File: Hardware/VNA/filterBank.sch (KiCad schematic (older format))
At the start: 18 parts, among them U10 SN74LVC1G139, U11 PE42440, U8 74AHC1G04, U9 PE42440

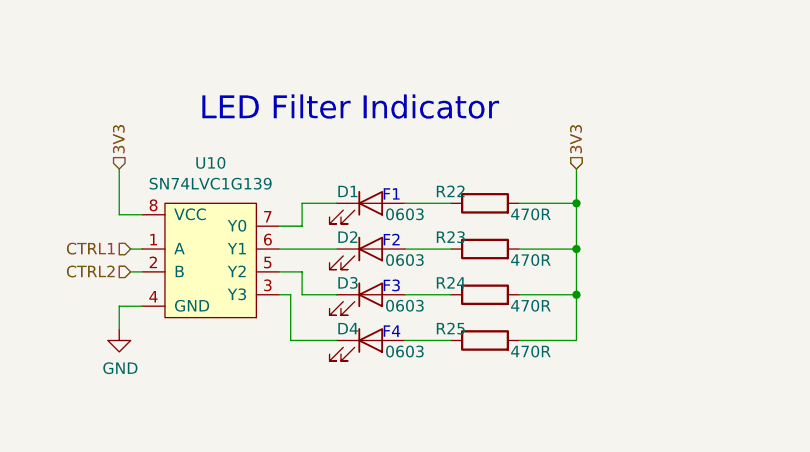
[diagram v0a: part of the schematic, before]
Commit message: added footprints and 3d models
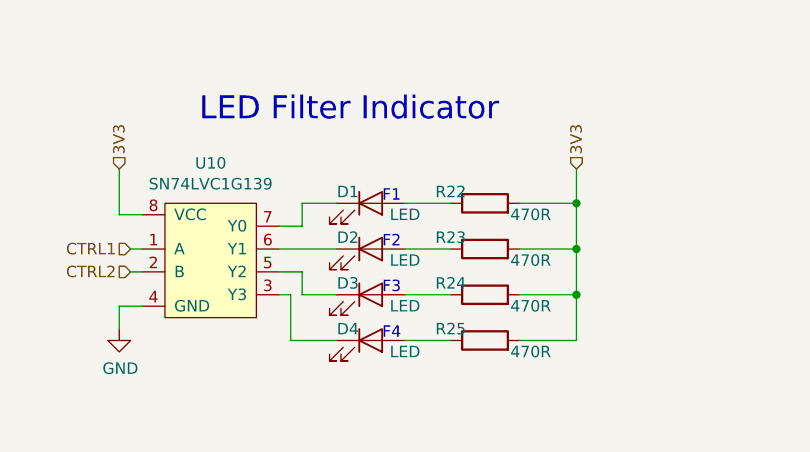
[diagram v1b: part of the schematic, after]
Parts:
- D1, D2, D3, D4: value 0603 -> LED; footprint (none) -> LED_SMD:LED_0603_1608Metric
- R22, R23, R24, R25: footprint (none) -> Resistor_SMD:R_0603_1608Metric
- U10: footprint (none) -> VNA_Footprints:VSSOP-8_2.9x3.15mm_P0.65
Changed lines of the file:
@@
 	8100 3150 8200 3150
 $Comp
-L power:GND #PWR061
+L power:GND #PWR060
 U 1 1 5C2A3D55
 P 8700 3200
-F 0 "#PWR061" H 8700 2950 50  0001 C CNN
+F 0 "#PWR060" H 8700 2950 50  0001 C CNN
 F 1 "GND" H 8705 3027 50  0000 C CNN
 F 2 "" H 8700 3200 50  0001 C CNN
@@
 	8750 1850 8750 1950
 $Comp
-L power:GND #PWR062
+L power:GND #PWR061
 U 1 1 5C2A413F
 P 8750 1950
-F 0 "#PWR062" H 8750 1700 50  0001 C CNN
+F 0 "#PWR061" H 8750 1700 50  0001 C CNN
 F 1 "GND" H 8755 1777 50  0000 C CNN
 F 2 "" H 8750 1950 50  0001 C CNN
@@
 	3600 3100 3500 3100
 $Comp
-L power:GND #PWR054
+L power:GND #PWR053
 U 1 1 5C2A4744
 P 3000 3150
-F 0 "#PWR054" H 3000 2900 50  0001 C CNN
+F 0 "#PWR053" H 3000 2900 50  0001 C CNN
 F 1 "GND" H 3005 2977 50  0000 C CNN
 F 2 "" H 3000 3150 50  0001 C CNN
@@
 	3550 1800 3550 1900
 $Comp
-L power:GND #PWR055
+L power:GND #PWR054
 U 1 1 5C2A475D
 P 3550 1900
-F 0 "#PWR055" H 3550 1650 50  0001 C CNN
+F 0 "#PWR054" H 3550 1650 50  0001 C CNN
 F 1 "GND" H 3555 1727 50  0000 C CNN
 F 2 "" H 3550 1900 50  0001 C CNN
@@
 	1500 7100 1500 7200
 $Comp
-L power:GND #PWR053
+L power:GND #PWR052
 U 1 1 5C2BF9CA
 P 1500 7200
-F 0 "#PWR053" H 1500 6950 50  0001 C CNN
+F 0 "#PWR052" H 1500 6950 50  0001 C CNN
 F 1 "GND" H 1505 7027 50  0000 C CNN
 F 2 "" H 1500 7200 50  0001 C CNN
@@
 	5250 2550 5250 2600
 $Comp
-L power:GND #PWR057
+L power:GND #PWR056
 U 1 1 5C3B9385
 P 5250 2600
-F 0 "#PWR057" H 5250 2350 50  0001 C CNN
+F 0 "#PWR056" H 5250 2350 50  0001 C CNN
 F 1 "GND" H 5255 2427 50  0000 C CNN
 F 2 "" H 5250 2600 50  0001 C CNN
@@
 	5250 3250 5250 3300
 $Comp
-L power:GND #PWR058
+L power:GND #PWR057
 U 1 1 5C3B9438
 P 5250 3300
-F 0 "#PWR058" H 5250 3050 50  0001 C CNN
+F 0 "#PWR057" H 5250 3050 50  0001 C CNN
 F 1 "GND" H 5255 3127 50  0000 C CNN
 F 2 "" H 5250 3300 50  0001 C CNN
@@
 	5250 3950 5250 4000
 $Comp
-L power:GND #PWR059
+L power:GND #PWR058
 U 1 1 5C3BCF2E
 P 5250 4000
-F 0 "#PWR059" H 5250 3750 50  0001 C CNN
+F 0 "#PWR058" H 5250 3750 50  0001 C CNN
 F 1 "GND" H 5255 3827 50  0000 C CNN
 F 2 "" H 5250 4000 50  0001 C CNN
@@
 	5250 4700 5250 4750
 $Comp
-L power:GND #PWR060
+L power:GND #PWR059
 U 1 1 5C3C0D3B
 P 5250 4750
-F 0 "#PWR060" H 5250 4500 50  0001 C CNN
+F 0 "#PWR059" H 5250 4500 50  0001 C CNN
 F 1 "GND" H 5255 4577 50  0000 C CNN
 F 2 "" H 5250 4750 50  0001 C CNN
@@
 F 0 "U10" H 4600 7325 50  0000 C CNN
 F 1 "SN74LVC1G139" H 4600 7234 50  0000 C CNN
-F 2 "" H 4700 7150 100 0001 C CNN
+F 2 "VNA_Footprints:VSSOP-8_2.9x3.15mm_P0.65" H 4700 7150 100 0001 C CNN
 F 3 "" H 4700 7150 100 0001 C CNN
 	1    4600 6900
@@
 	4200 7100 4200 7200
 $Comp
-L power:GND #PWR056
+L power:GND #PWR055
 U 1 1 5CE265C0
 P 4200 7200
-F 0 "#PWR056" H 4200 6950 50  0001 C CNN
+F 0 "#PWR055" H 4200 6950 50  0001 C CNN
 F 1 "GND" H 4205 7027 50  0000 C CNN
 F 2 "" H 4200 7200 50  0001 C CNN
@@
 F 0 "R22" V 5850 6800 50  0000 C CNN
 F 1 "470R" V 5750 6450 50  0000 C CNN
-F 2 "" V 5730 6650 50  0001 C CNN
+F 2 "Resistor_SMD:R_0603_1608Metric" V 5730 6650 50  0001 C CNN
 F 3 "~" H 5800 6650 50  0001 C CNN
 	1    5800 6650
@@
 P 5300 6650
 F 0 "D1" H 5200 6700 50  0000 C CNN
-F 1 "0603" H 5450 6600 50  0000 C CNN
-F 2 "" H 5300 6650 50  0001 C CNN
+F 1 "LED" H 5450 6600 50  0000 C CNN
+F 2 "LED_SMD:LED_0603_1608Metric" H 5300 6650 50  0001 C CNN
 F 3 "~" H 5300 6650 50  0001 C CNN
 	1    5300 6650
@@
 P 5300 6850
 F 0 "D2" H 5200 6900 50  0000 C CNN
-F 1 "0603" H 5450 6800 50  0000 C CNN
-F 2 "" H 5300 6850 50  0001 C CNN
+F 1 "LED" H 5450 6800 50  0000 C CNN
+F 2 "LED_SMD:LED_0603_1608Metric" H 5300 6850 50  0001 C CNN
 F 3 "~" H 5300 6850 50  0001 C CNN
 	1    5300 6850
@@
 P 5300 7050
 F 0 "D3" H 5200 7100 50  0000 C CNN
-F 1 "0603" H 5450 7000 50  0000 C CNN
-F 2 "" H 5300 7050 50  0001 C CNN
+F 1 "LED" H 5450 7000 50  0000 C CNN
+F 2 "LED_SMD:LED_0603_1608Metric" H 5300 7050 50  0001 C CNN
 F 3 "~" H 5300 7050 50  0001 C CNN
 	1    5300 7050
@@
 P 5300 7250
 F 0 "D4" H 5200 7300 50  0000 C CNN
-F 1 "0603" H 5450 7200 50  0000 C CNN
-F 2 "" H 5300 7250 50  0001 C CNN
+F 1 "LED" H 5450 7200 50  0000 C CNN
+F 2 "LED_SMD:LED_0603_1608Metric" H 5300 7250 50  0001 C CNN
 F 3 "~" H 5300 7250 50  0001 C CNN
 	1    5300 7250
@@
 F 0 "R23" V 5850 7000 50  0000 C CNN
 F 1 "470R" V 5750 6650 50  0000 C CNN
-F 2 "" V 5730 6850 50  0001 C CNN
+F 2 "Resistor_SMD:R_0603_1608Metric" V 5730 6850 50  0001 C CNN
 F 3 "~" H 5800 6850 50  0001 C CNN
 	1    5800 6850
@@
 F 0 "R24" V 5850 7200 50  0000 C CNN
 F 1 "470R" V 5750 6850 50  0000 C CNN
-F 2 "" V 5730 7050 50  0001 C CNN
+F 2 "Resistor_SMD:R_0603_1608Metric" V 5730 7050 50  0001 C CNN
 F 3 "~" H 5800 7050 50  0001 C CNN
 	1    5800 7050
@@
 F 0 "R25" V 5850 7400 50  0000 C CNN
 F 1 "470R" V 5750 7050 50  0000 C CNN
-F 2 "" V 5730 7250 50  0001 C CNN
+F 2 "Resistor_SMD:R_0603_1608Metric" V 5730 7250 50  0001 C CNN
 F 3 "~" H 5800 7250 50  0001 C CNN
 	1    5800 7250

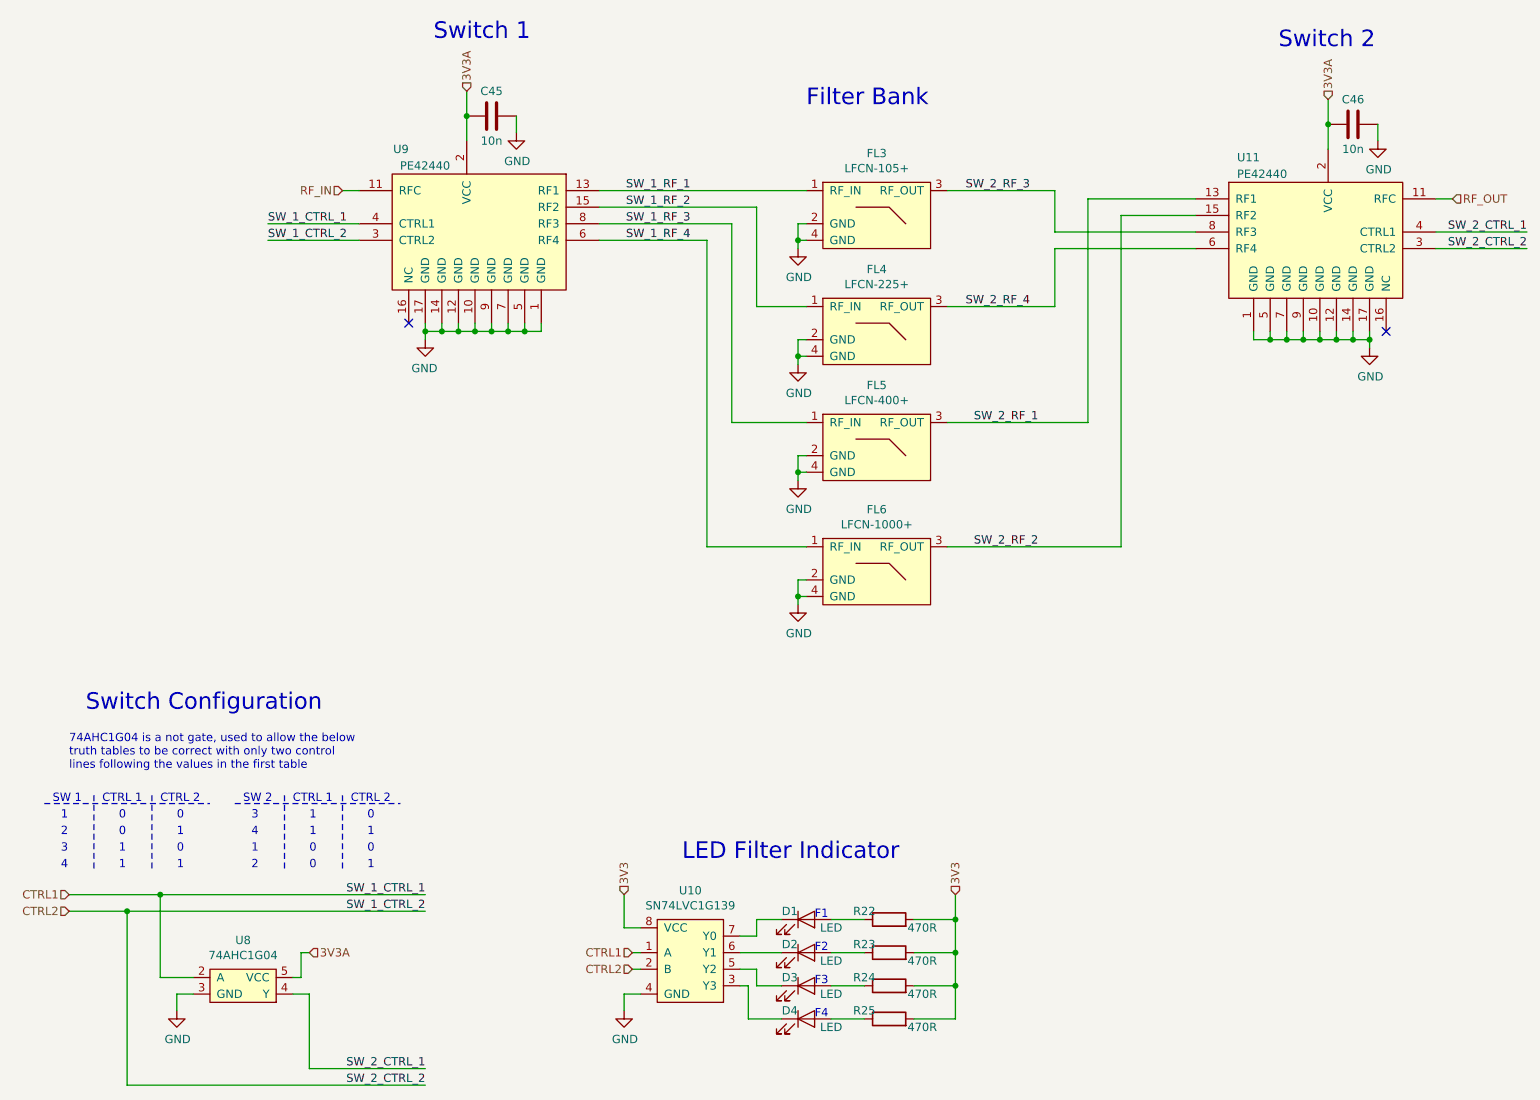
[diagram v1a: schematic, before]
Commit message: prelim schematic capture complete
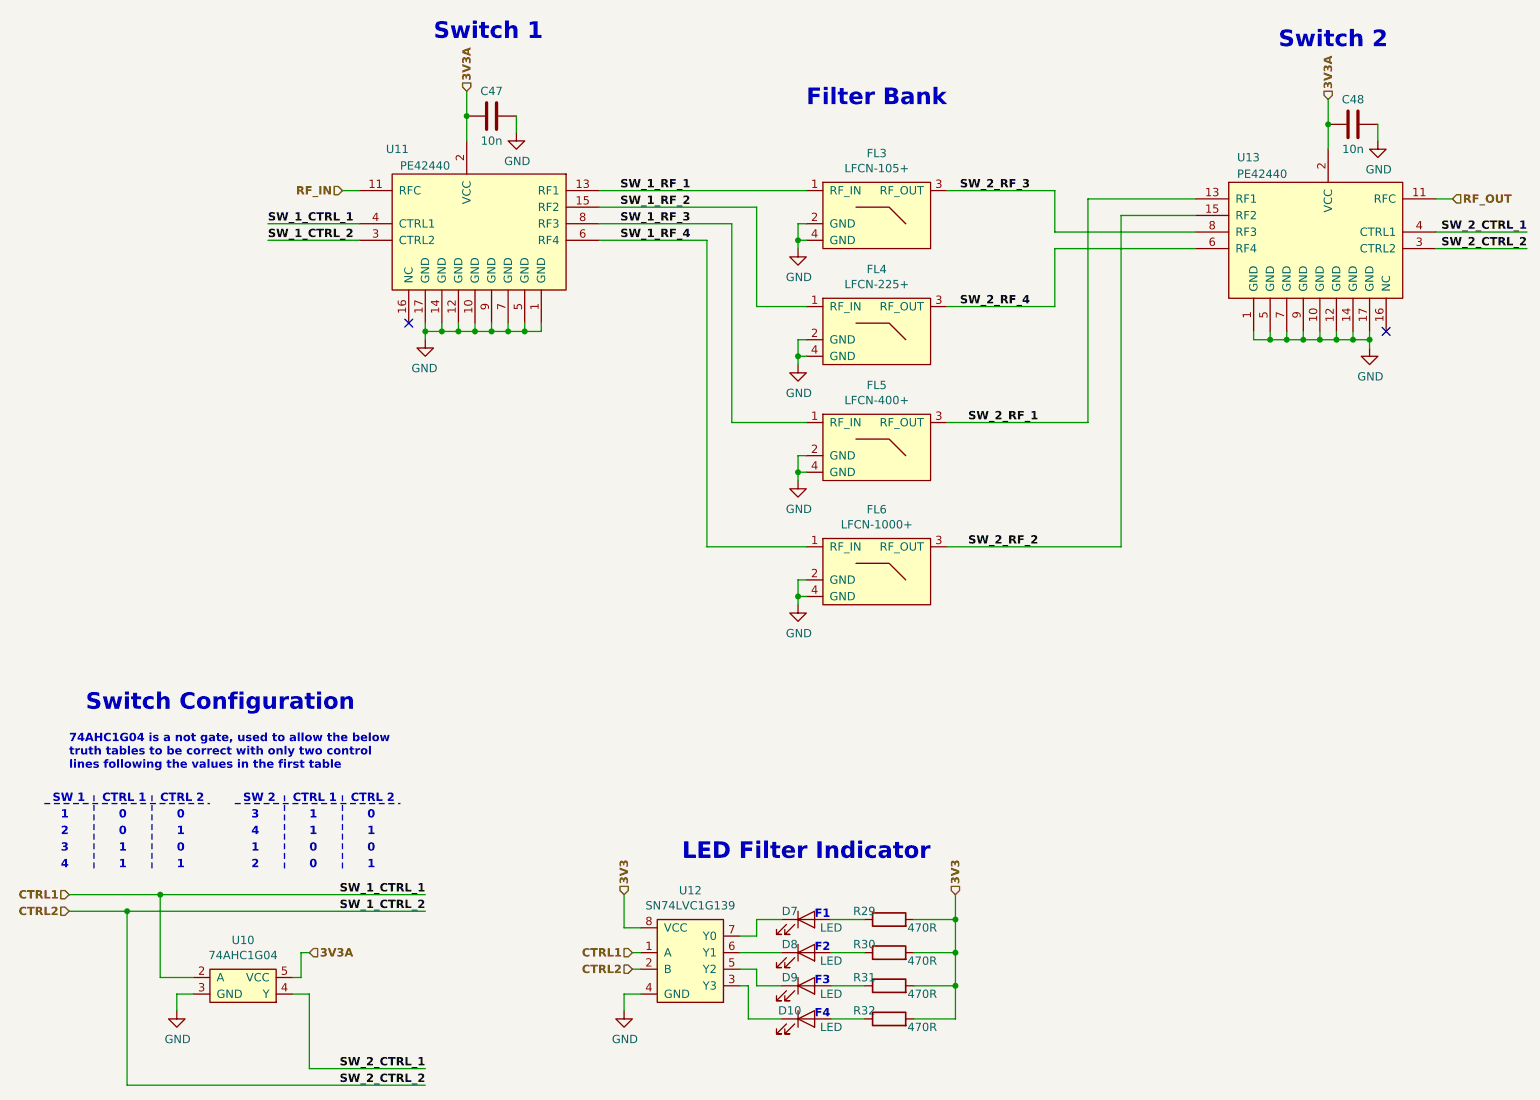
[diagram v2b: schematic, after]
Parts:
- renumbered C45 to C47, C46 to C48, D4 to D10, D1 to D7, D2 to D8, D3 to D9, R22 to R29, R23 to R30, R24 to R31, R25 to R32, U8 to U10, U9 to U11, U10 to U12, U11 to U13
